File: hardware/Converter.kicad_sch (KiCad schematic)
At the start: 79 parts, among them J4 VIOUT, J5 VIIN, Q1 BUK9M53-60EX, Q2 BUK9M53-60EX, Q3 BUK9M53-60EX, Q4 BUK9M53-60EX

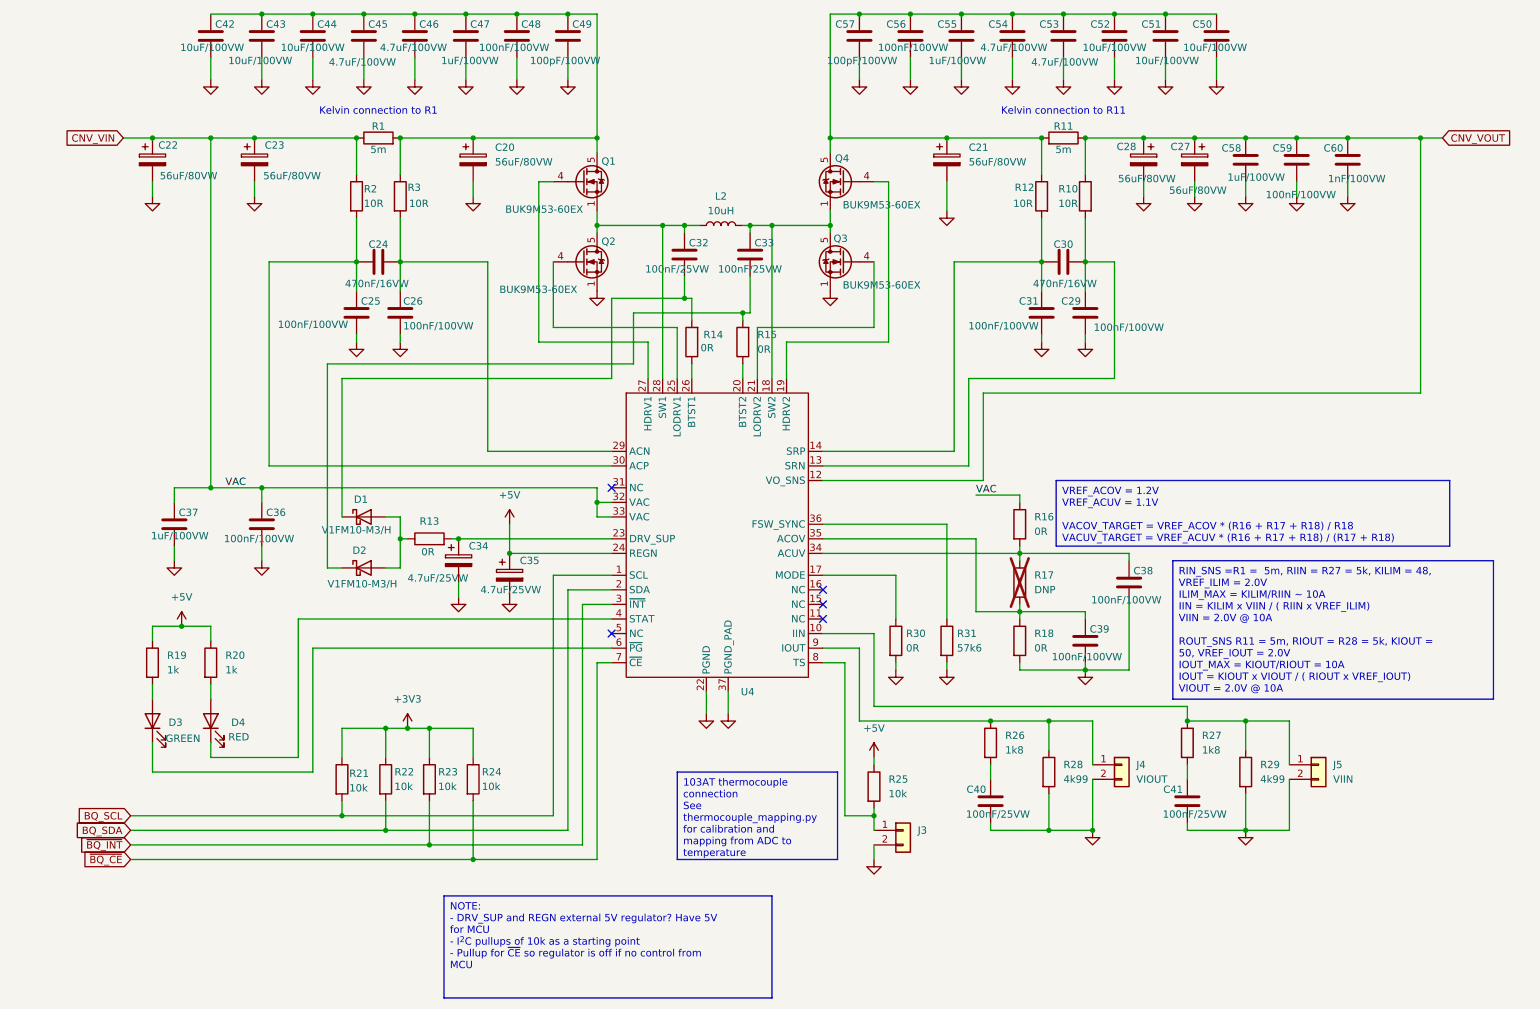
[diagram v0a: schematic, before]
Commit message: WIP checkin * Added most of the JLCPCB part numbers * Added most of the component footprints * Connected up microcontroller and dc/dc converter
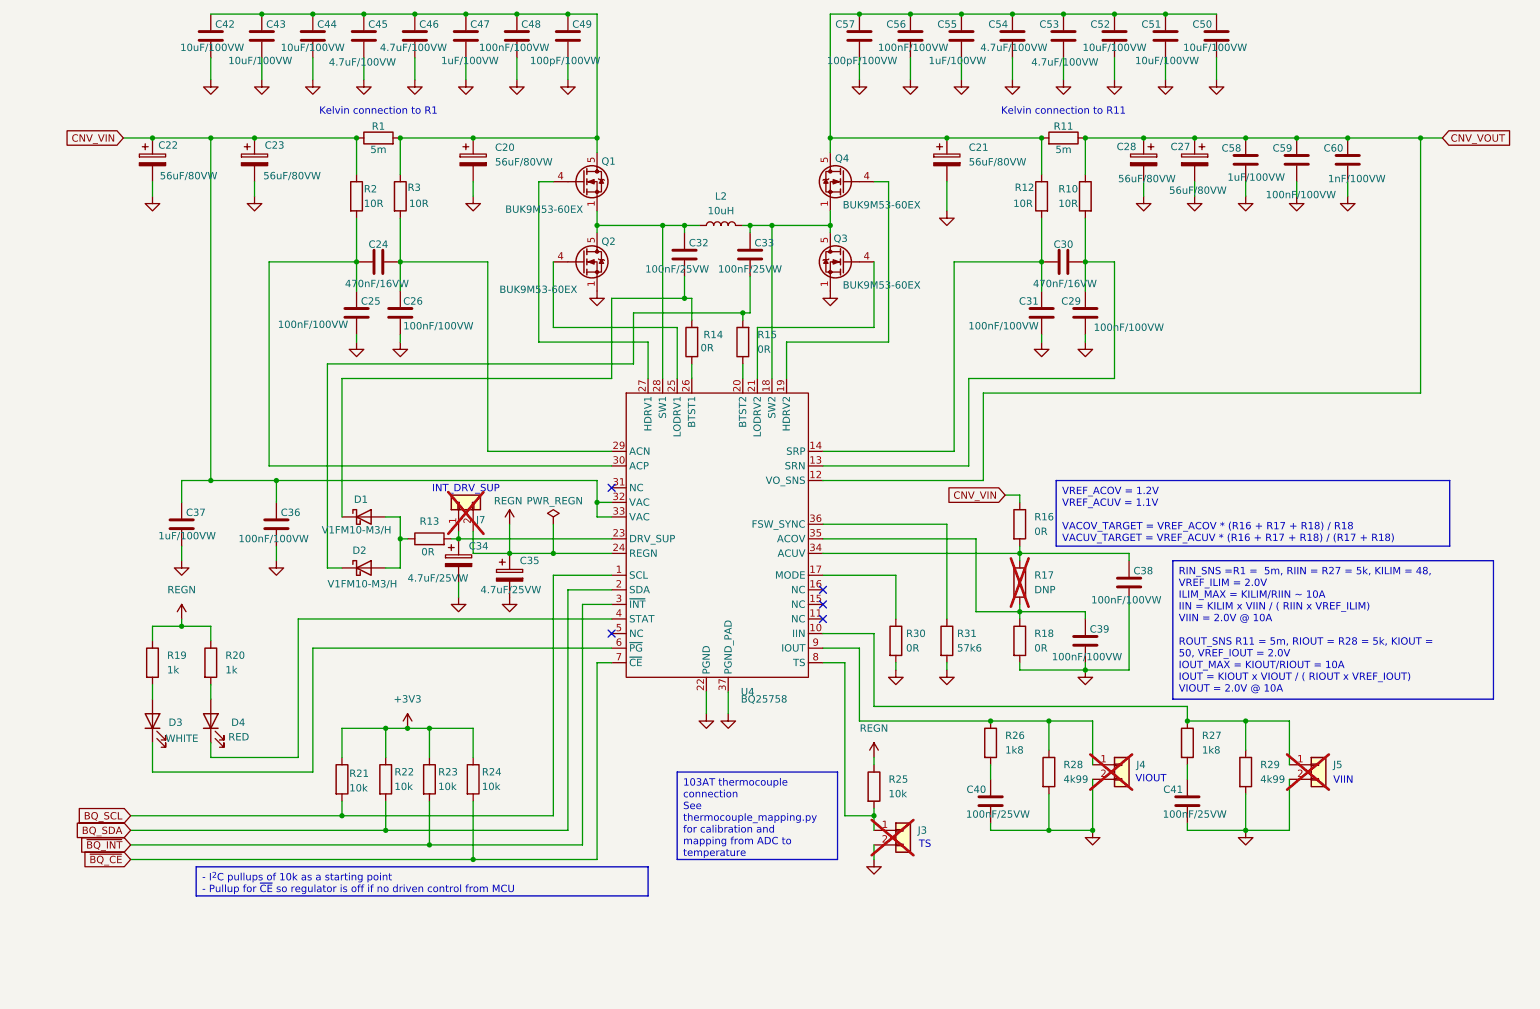
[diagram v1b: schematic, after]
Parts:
- added J7: CON2, Connector_PinHeader_2.54mm:PinHeader_1x02_P2.54mm_Vertical, symbol Connector_Generic:Conn_01x02
- C20, C21, C22, C23, C27, C28: footprint (none) -> Capacitor_SMD:CP_Elec_10x10.5; JLCPCB (none) -> C128515
- C24, C30: footprint (none) -> Capacitor_SMD:C_0603_1608Metric; JLCPCB (none) -> C1623
- C25, C26, C29, C31, C36, C38, C39, C48, C56, C59: footprint (none) -> Capacitor_SMD:C_1206_3216Metric; JLCPCB (none) -> C1945
- C32, C33, C40, C41: footprint (none) -> Capacitor_SMD:C_0603_1608Metric; JLCPCB (none) -> C1590
- C34, C35: footprint (none) -> Capacitor_SMD:C_0805_2012Metric; JLCPCB (none) -> C1779
- C37, C47, C55, C58: footprint (none) -> Capacitor_SMD:C_1206_3216Metric; JLCPCB (none) -> C13832
- C42, C43, C44, C50, C51, C52: footprint (none) -> Capacitor_SMD:CP_Elec_6.3x7.7; JLCPCB (none) -> C19077968
- C45, C46, C53, C54: footprint (none) -> Capacitor_SMD:CP_Elec_6.3x7.7; JLCPCB (none) -> C970653
- C49, C57: footprint (none) -> Capacitor_SMD:C_0805_2012Metric; JLCPCB (none) -> C37456
- C60: footprint (none) -> Capacitor_SMD:C_0805_2012Metric; JLCPCB (none) -> C15177
- D1, D2: footprint (none) -> Diode_SMD:D_SMF; JLCPCB (none) -> C3758930
- D3: value GREEN -> WHITE; JLCPCB (none) -> C2290
- D4: JLCPCB (none) -> C2286
- J3: value ~ -> CON2; footprint (none) -> Connector_PinHeader_2.54mm:PinHeader_1x02_P2.54mm_Vertical; now not fitted
- J4: value VIOUT -> CON2; footprint (none) -> Connector_PinHeader_2.54mm:PinHeader_1x02_P2.54mm_Vertical; now not fitted
- J5: value VIIN -> CON2; footprint (none) -> Connector_PinHeader_2.54mm:PinHeader_1x02_P2.54mm_Vertical; now not fitted
- L2: footprint (none) -> Inductor_SMD:L_Wuerth_HCM-1350; JLCPCB (none) -> C17459880
- R1, R11: footprint (none) -> Resistor_SMD:R_2512_6332Metric; JLCPCB (none) -> C49483
- R10, R12, R2, R3: footprint (none) -> Resistor_SMD:R_0603_1608Metric; JLCPCB (none) -> C22859
- R13, R14, R15, R16, R18, R30: footprint (none) -> Resistor_SMD:R_0603_1608Metric; JLCPCB (none) -> C21189
- R17: footprint (none) -> Resistor_SMD:R_0603_1608Metric
- R19, R20: footprint (none) -> Resistor_SMD:R_0603_1608Metric; JLCPCB (none) -> C21190
- R21, R22, R23, R24, R25: footprint (none) -> Resistor_SMD:R_0603_1608Metric; JLCPCB (none) -> C25804
- R26, R27: footprint (none) -> Resistor_SMD:R_0603_1608Metric; JLCPCB (none) -> C4177
- R28, R29: footprint (none) -> Resistor_SMD:R_0603_1608Metric; JLCPCB (none) -> C2692815
- R31: footprint (none) -> Resistor_SMD:R_0603_1608Metric; JLCPCB (none) -> C23082
- U4: value ~ -> BQ25758; footprint (none) -> BidirectionalSupply:QFN-36_L6.0-W5.0-P0.50-BL-EP-1; JLCPCB (none) -> C33222334
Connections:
- net at C34.1, R13.2, U4.23 (DRV_SUP): now also J7.1 (Pin_1)
- net +5V renamed REGN
- net REGN: now also J7.2 (Pin_2)
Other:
- note added: "INT_DRV_SUP"
- note added: "TS"
- note added: "VIIN"
- note added: "VIOUT"
- company: (none) -> Open Source Solutions Pty Ltd
- title: (none) -> Converter
- moved on the sheet: C36, C37

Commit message: Schematic is now mostly complete. Will review and then move onto the PCB layout
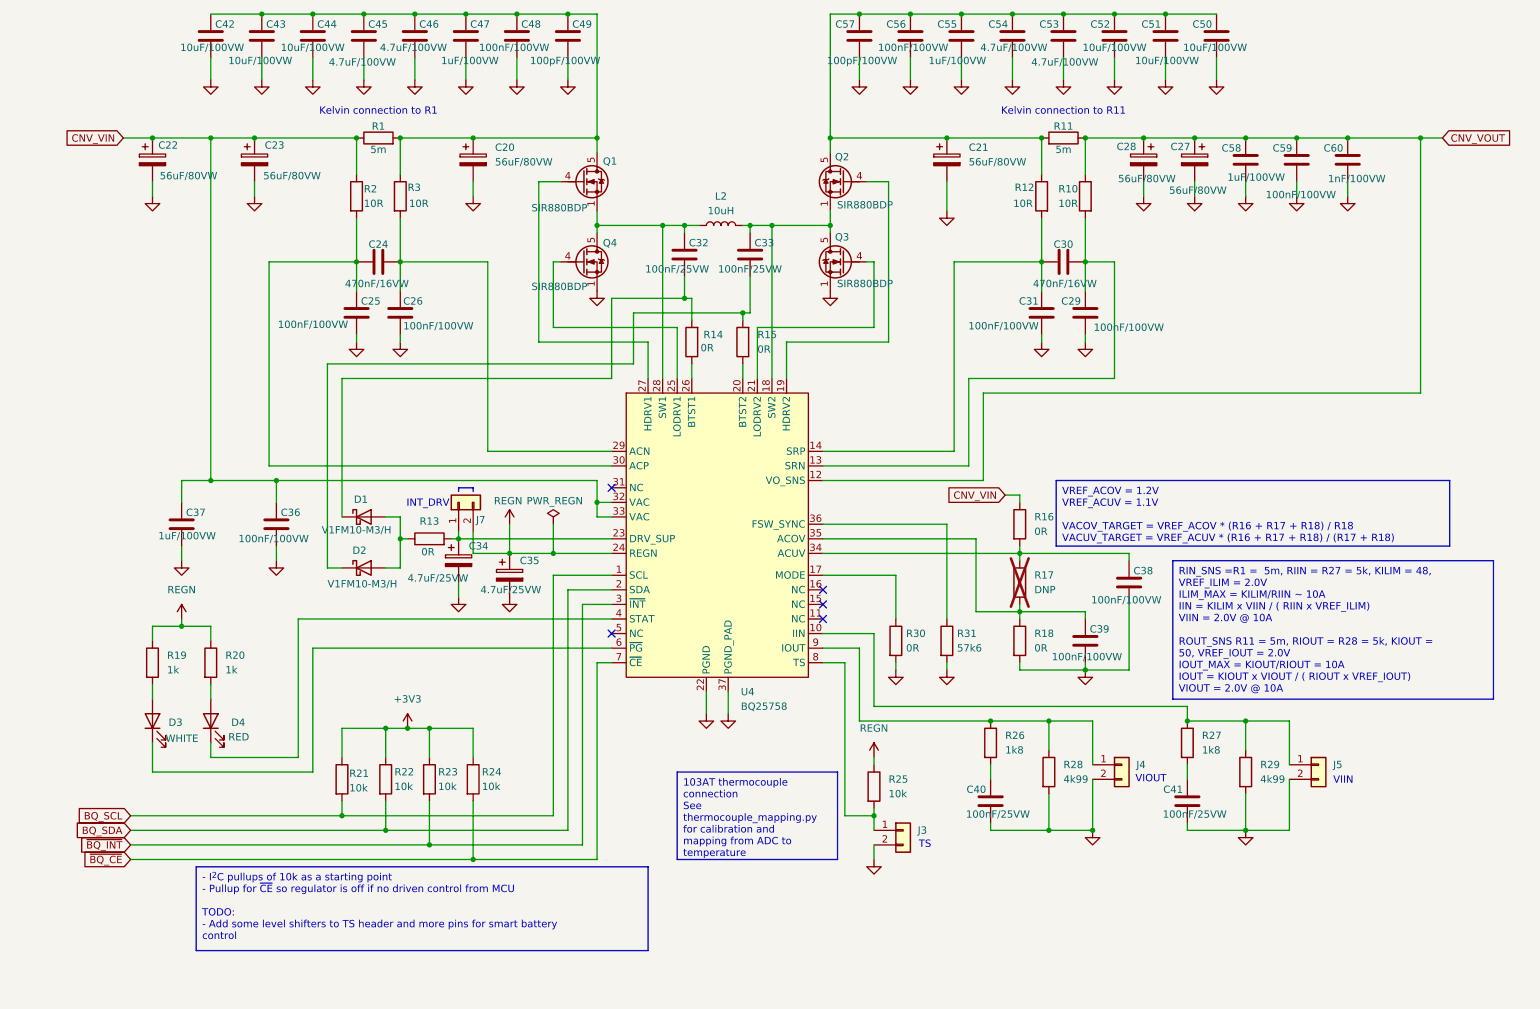
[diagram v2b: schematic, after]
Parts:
- removed Q1, Q2, Q3, Q4: BUK9M53-60EX, Package_TO_SOT_SMD:LFPAK33, symbol BC-lib:BUK7Y4R8-60E
- added Q1, Q2, Q3, Q4: SIR880BDP, BidirectionalSupply:POWERPAK-SO-8_L6.2-W5.2-P1.27-BL-EP, symbol BidirectionalSupply:SIR880BDP
- J3, J4, J5, J7: now fitted
- U4: symbol BC-lib:BQ25758 -> BidirectionalSupply:BQ25758
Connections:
- net GND: now also Q3.1 (S), Q3.2 (S), Q3.3 (S), Q4.1 (S), Q4.2 (S), Q4.3 (S)
- net at U4.25 (LODRV1): now also Q4.4 (G)
- net at C32.1, L2.1, U4.28 (SW1): now also Q1.1 (S), Q1.2 (S), Q1.3 (S), Q4.5 (D), Q4.6 (D), Q4.7 (D), Q4.8 (D), Q4.9 (EP)
- net at C20.1, C42.1, C43.1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: now also Q1.5 (D), Q1.6 (D), Q1.7 (D), Q1.8 (D), Q1.9 (EP)
- net at C21.1, C50.1, C51.1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: now also Q2.5 (D), Q2.6 (D), Q2.7 (D), Q2.8 (D), Q2.9 (EP)
- net at C33.1, L2.2, U4.18 (SW2): now also Q2.1 (S), Q2.2 (S), Q2.3 (S), Q3.5 (D), Q3.6 (D), Q3.7 (D), Q3.8 (D), Q3.9 (EP)
- net at U4.19 (HDRV2): now also Q2.4 (G)
- net at U4.21 (LODRV2): now also Q3.4 (G)
- net at U4.27 (HDRV1): now also Q1.4 (G)
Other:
- note added: "INT_DRV"
- note removed: "INT_DRV_SUP"

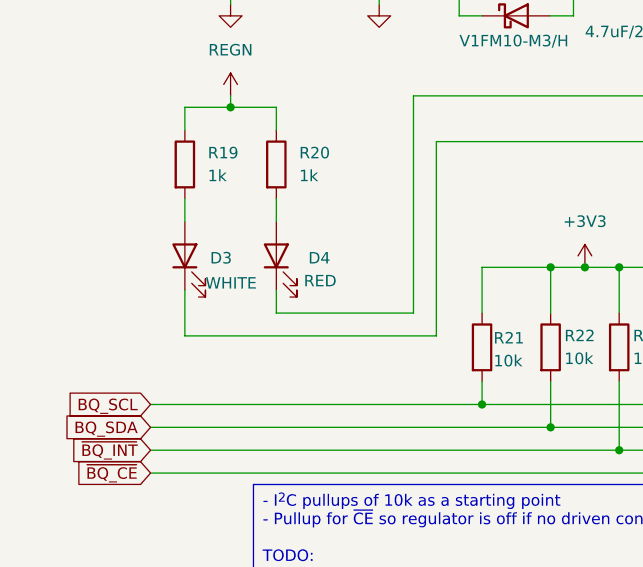
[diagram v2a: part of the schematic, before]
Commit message: Checked all DC/DC converter capacitors Some part substitution to preference in stock items
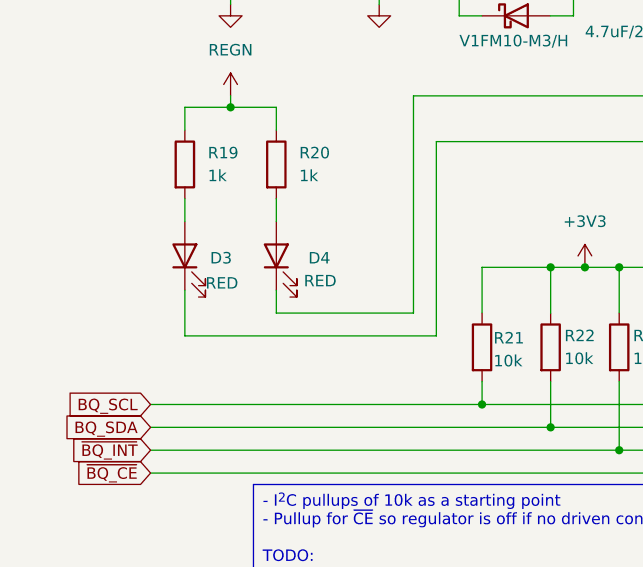
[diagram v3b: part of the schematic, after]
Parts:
- D3: value WHITE -> RED; JLCPCB C2290 -> C2286
- L2: JLCPCB C17459880 -> (none); Mouser (none) -> 530-SCIHP1367-100M
- R1, R11: footprint Resistor_SMD:R_2512_6332Metric -> BidirectionalSupply:RES-SMD_L10.0-W5.2; JLCPCB C49483 -> C481477
